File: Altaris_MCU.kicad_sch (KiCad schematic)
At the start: 47 parts, among them J1 Screw_Terminal_01x02, J2 Conn_01x04_Pin, J3 Screw_Terminal_01x02, J4 Screw_Terminal_01x02, J5 Conn_01x04_Pin, J6 Conn_01x04_Pin, J7 Conn_01x08_Socket, SW2 RESET1, SW3 BOOT1, U1 ESP32-S3-WROOM-1, U2 MAX31855KASA, U3 TPS79333-EP, U4 ICM-20948, U5 TPS79318-EP, U6 SN74AVC4T774RSVR, U7 MAX31855KASA, U8 MAX31855KASA

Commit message: Added USB-C to Schematic and PCB Layout
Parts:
- added C24, C25: 0.1uF, Capacitor_SMD:C_0402_1005Metric_Pad0.74x0.62mm_HandSolder, symbol Device:C
- added C26, C29: 100n, Capacitor_SMD:C_0402_1005Metric, symbol Device:C
- added C27, C28, C30: 10u, Capacitor_SMD:C_0402_1005Metric, symbol Device:C
- added FB3: 600/100, Resistor_SMD:R_0805_2012Metric, symbol Device:R
- added J8: Screw_Terminal_01x02, TerminalBlock:TerminalBlock_MaiXu_MX126-5.0-02P_1x02_P5.00mm, symbol Connector:Screw_Terminal_01x02
- added J9: USB_C_Receptacle_USB2.0_16P, Connector_USB:USB_C_Receptacle_HRO_TYPE-C-31-M-12, symbol Connector:USB_C_Receptacle_USB2.0_16P
- added R4, R5: 5.1k, Resistor_SMD:R_0402_1005Metric, symbol Device:R
- added U10: USBLC6-2SC6, Package_TO_SOT_SMD:SOT-23-6, symbol Power_Protection:USBLC6-2SC6
- added U11: SPX3819M5-L-3-3, Package_TO_SOT_SMD:SOT-23-5, symbol Regulator_Linear:SPX3819M5-L-3-3
- added U9: SN74AVC4T774RSVR, MyFootprints:RSV0016A, symbol SN74AVC4T774RSVR:SN74AVC4T774RSVR
- C1, C10, C15, C22, C23, C4, C5, C6, C7, C8, C9: footprint Capacitors:C_0805_2012Metric_Pad1.18x1.45mm_HandSolder -> Capacitor_SMD:C_0805_2012Metric_Pad1.18x1.45mm_HandSolder
- J1, J3, J4: footprint (none) -> TerminalBlock:TerminalBlock_MaiXu_MX126-5.0-02P_1x02_P5.00mm
- J2, J5, J6: footprint (none) -> TerminalBlock:TerminalBlock_MaiXu_MX126-5.0-04P_1x04_P5.00mm
- U4: footprint ICM-20948:QFN24_3X3X0P9_IVS -> MyFootprints:QFN24_3X3X0P9_IVS
- U6: footprint LEVELSHIFTER:QFN40P260X180X55-16N -> MyFootprints:RSV0016A
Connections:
- net T+ is gone; now on net T1+: U7.3 (T+)
- net T- is gone; now on net T1-: U7.2 (T-)
- net +1.8V: now also C25.1, U9.13 (VCCB)
- net +3.3V_b: now also R10.2, R9.2, C24.1, C30.1, U11.5 (OUT), U9.14 (VCCA), U9.16 (DIR2), U9.5 (DIR3), U9.6 (DIR4)
- net +5V_b: now also J8.1 (Pin_1)
- net ADC_IN1: now also U1.24 (IO47); no longer U1.39 (IO1)
- net ADC_IN2: now also U1.25 (IO48); no longer U1.38 (IO2)
- net ADC_IN3: now also U1.26 (IO45); no longer U1.15 (IO3)
- net CLK: now also U1.35 (IO42); no longer U1.22 (IO14)
- net ESP32_EN: now also C18.1, R9.1
- net GND: now also C24.2, C25.2, C26.2, C27.2, C28.2, C29.2, C30.2, J8.2 (Pin_2), J9.A1 (GND), J9.A12 (GND), J9.B1 (GND), J9.B12 (GND), J9.S1 (SHIELD), R4.2, R5.2, U10.2 (GND), U11.2 (GND), U9.15 (DIR1), U9.7 (~{OE}), U9.8 (GND)
- net GPIO0: now also C19.1, R10.1
- net ICM_CS: now also U1.38 (IO2); no longer U1.8 (IO15)
- net ICM_FSYNC: now also U1.33 (IO40), U9.1 (A1); no longer U1.9 (IO16)
- net ICM_FSYNC_1.8V: now also U9.12 (B1)
- net ICM_INT: now also U1.32 (IO39), U9.2 (A2); no longer U1.19 (IO11)
- net ICM_INT_1.8V: now also U9.11 (B2)
- net MAX_CS2: now also U1.18 (IO10); no longer U1.12 (IO8)
- net MAX_CS3: now also U1.19 (IO11); no longer U1.18 (IO10)
- net MISO: now also U1.39 (IO1); no longer U1.20 (IO12)
- net MOSI: now also U1.34 (IO41); no longer U1.21 (IO13)
- net T1-: no longer U2.2 (T-)
- net T2-: now also U2.2 (T-)
- net Common2: now reaches J2.2 (Pin_2)
- net Common3: now reaches J5.2 (Pin_2)
- net Common1: now reaches J6.2 (Pin_2)
- net USB-: now reaches U1.13 (USB_D-)
- net USB-: now also U10.6 (I/O1)
- net USB+: now reaches U1.14 (USB_D+)
- net USB+: now also U10.4 (I/O2)
- new net: J9.B5 (CC2), R4.1
- new net: C29.1, U11.4 (BP)
- new net: J9.A5 (CC1), R5.1
- new net: J9.A7 (D-), J9.B7 (D-), U10.1 (I/O1)
- new net: J9.A6 (D+), J9.B6 (D+), U10.3 (I/O2)
- new net +VBUS: C26.1, FB3.2, J9.A4 (VBUS), J9.A9 (VBUS), J9.B4 (VBUS), J9.B9 (VBUS), U10.5 (VBUS)
- new net +VBUSF: C27.1, C28.1, FB3.1, U11.1 (IN), U11.3 (EN)
- no-connect marks 24 -> 29
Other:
- moved on the sheet: C1, C10, C11, C12, C13, C14, C15, C16, C17, C18, C19, C2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

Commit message: Added Buck Converter to Schematic
USB-C BUS(5V) -> BUCK -> 3.3V -> (Voltage regulator to get 1.8V?)
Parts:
- added C31: 4.7u, Capacitor_SMD:C_0201_0603Metric, symbol Device:C
- added C32: 20u, Capacitor_SMD:C_0201_0603Metric, symbol Device:C
- added C33: 120p, Capacitor_SMD:C_0201_0603Metric, symbol Device:C
- added L1: L, Inductor_SMD:L_6.3x6.3_H3, symbol Device:L
- added R6, R8: 100k, Resistor_SMD:R_0402_1005Metric, symbol Device:R_Small
- added R7: 450k, Resistor_SMD:R_0402_1005Metric, symbol Device:R_Small
- added U12: TPS62827DMQT, MyFootprints:DMQ0006A, symbol BuckConverter:TPS62827DMQT
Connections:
- net +3.3V_b: now also C32.1, C33.1, L1.2, R7.2
- net GND: now also C31.1, C32.2, C33.2, R7.1, R8.1, R8.2, U12.3 (FB), U12.4 (GND)
- new net: R6.1, U12.2 (PG)
- new net: L1.1, U12.5 (SW)
- new net VBUS: C31.2, R6.2, U12.1 (EN), U12.6 (VIN)
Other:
- moved on the sheet: C1, C10, C11, C12, C13, C16, C17, C24, C25, C4, C5, C6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

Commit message: added second USB port, labels, organize
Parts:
- added C39, C40, C41: 0.1uF, Capacitor_SMD:C_0402_1005Metric_Pad0.74x0.62mm_HandSolder, symbol Device:C
- added D1: 1N4148WT, Diode_SMD:D_SOD-523, symbol Diode:1N4148WT
- added J10: USB_C_Receptacle_USB2.0_16P, Connector_USB:USB_C_Receptacle_HRO_TYPE-C-31-M-12, symbol Connector:USB_C_Receptacle_USB2.0_16P
- added Q1: Q_NMOS, symbol Device:Q_NMOS
- added R13, R14: 5.1k, Resistor_SMD:R_0402_1005Metric, symbol Device:R
- added U15: CH340X, Package_SO:MSOP-10_3x3mm_P0.5mm, symbol Interface_USB:CH340X
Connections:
- net +3.3V_b: now also C41.2, Q1.G
- net +VBUS: now also C40.1, J10.A4 (VBUS), J10.A7 (D-), J10.A9 (VBUS), J10.B4 (VBUS), J10.B9 (VBUS), U15.7 (VCC)
- net GND: now also C39.1, C40.2, C41.1, J10.A1 (GND), J10.A12 (GND), J10.B1 (GND), J10.B12 (GND), J10.B6 (D+), J10.S1 (SHIELD), R13.2, R14.2, U15.3 (GND)
- net RXD0: now reaches U1.36 (RXD0)
- net RXD0: now also D1.2 (A)
- net TXD0: now reaches U1.37 (TXD0)
- net TXD0: now also Q1.S
- new net: J10.B5 (CC2), R13.1
- new net: C39.2, U15.10 (V3)
- new net: D1.1 (K), U15.8 (TXD)
- new net: Q1.D, U15.9 (RXD)
- new net: J10.A5 (CC1), R14.1
- new net UD+: J10.A6 (D+), U15.1 (UD+)
- new net UD-: J10.B7 (D-), U15.2 (UD-)
- no-connect marks 29 -> 32
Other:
- note added: "2SK3018"
- note added: "3871K519 Thermocouples"
- note added: "4/13/26"
- note added: "Debug"
- note added: "ESP 32"
- note added: "LDO Voltage Regulators"
- note added: "Level Shifters for IMU"
- note added: "Pressure Sensors"
- note added: "Standard Panel Jacks"
- note added: "Step-down Converter"
- note added: "Thermocouple-to-Digital Converters:"
- note added: "USB to Serial Port Chip"
- note added: "USB-C Ports"
- note removed: "3871K519 Thermocouple"
- note removed: "4/7/26"
- note removed: "ESP32"
- note removed: "Pressure Sensor"
- note removed: "Standard Panel Jack"
- moved on the sheet: C1, C10, C11, C12, C13, C14, C15, C16, C17, C20, C21, C22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

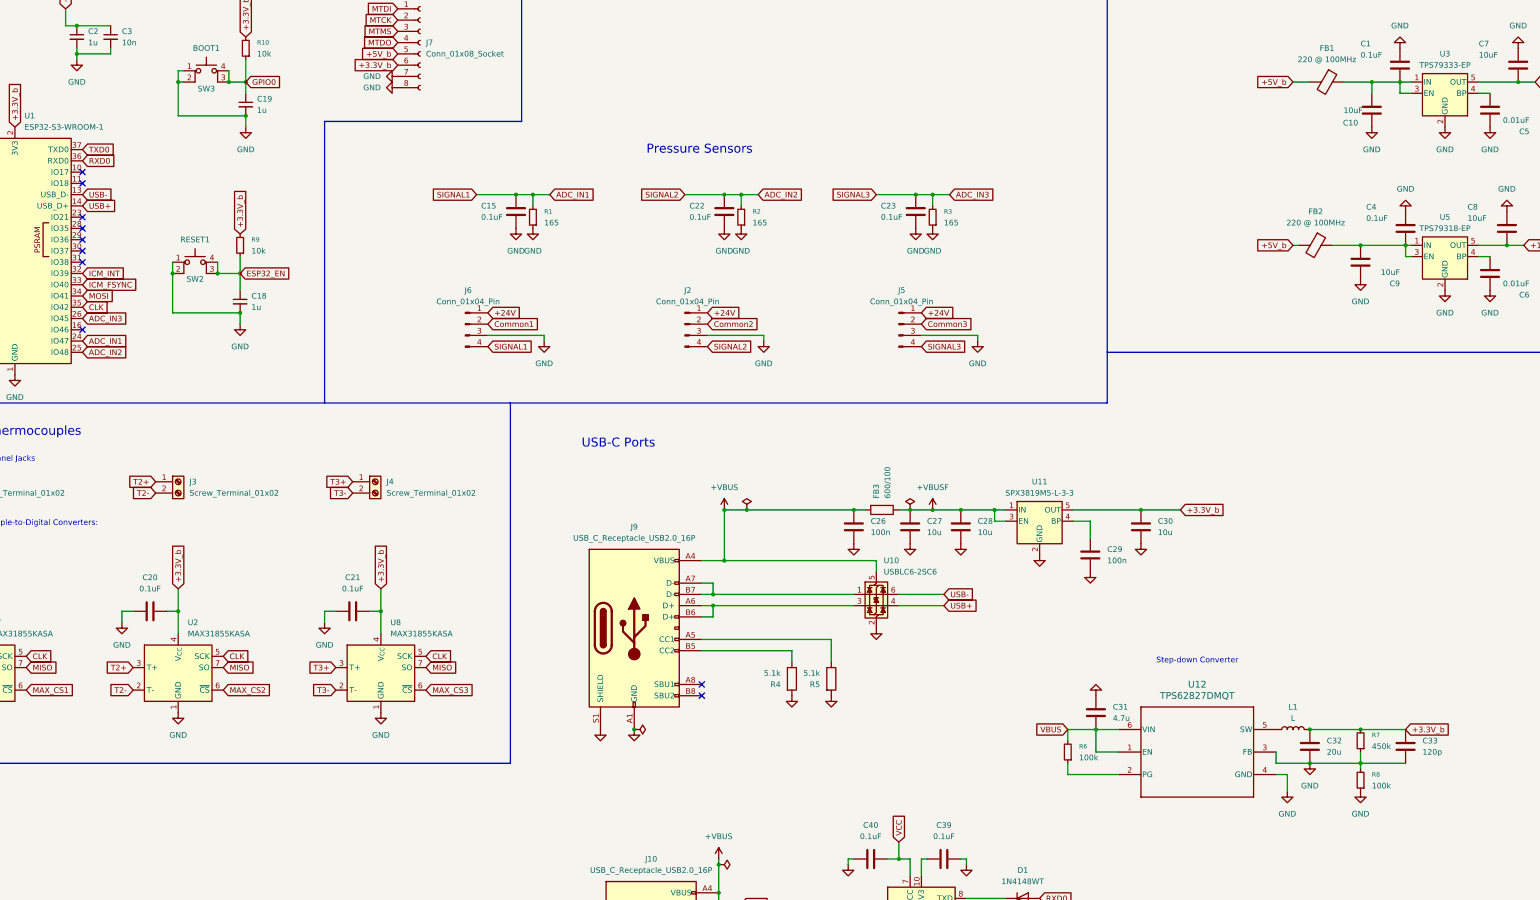
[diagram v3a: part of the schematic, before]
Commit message: Swapped LDO for Buck and added some test LED's
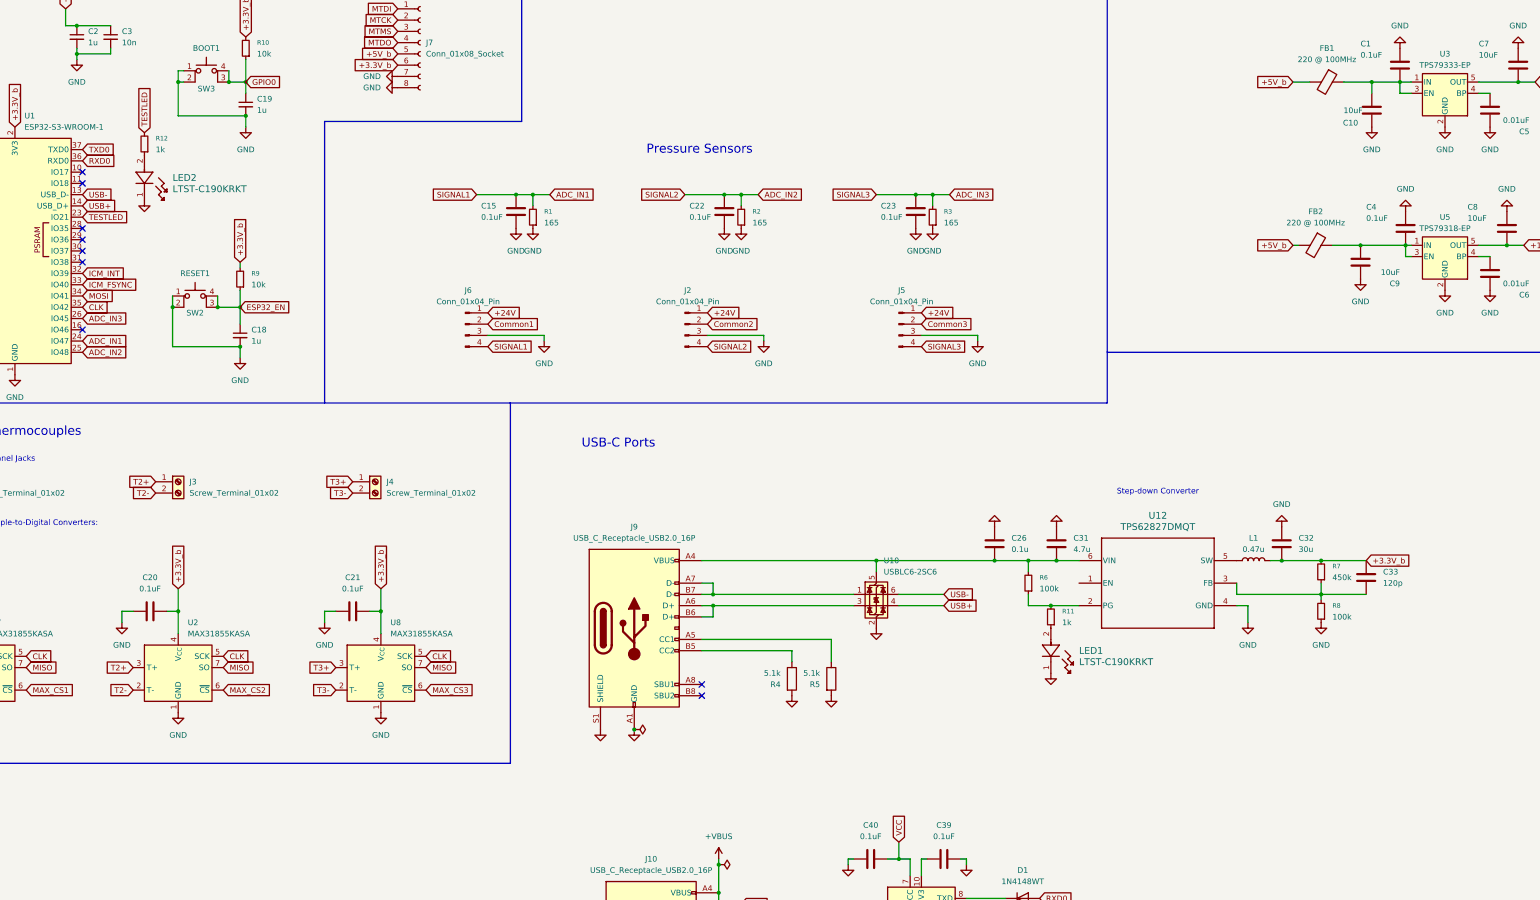
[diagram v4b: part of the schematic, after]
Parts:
- removed C27, C28, C30: 10u, Capacitor_SMD:C_0402_1005Metric, symbol Device:C
- removed C29: 100n, Capacitor_SMD:C_0402_1005Metric, symbol Device:C
- removed FB3: 600/100, Resistor_SMD:R_0805_2012Metric, symbol Device:R
- removed U11: SPX3819M5-L-3-3, Package_TO_SOT_SMD:SOT-23-5, symbol Regulator_Linear:SPX3819M5-L-3-3
- added LED1, LED2: LTST-C190KRKT, MyFootprints:LED_LTST-C190_LTO, symbol LED:LTST-C190KRKT
- added R11, R12: 1k, Resistor_SMD:R_0402_1005Metric, symbol Device:R_Small
- C26: value 100n -> 0.1u; footprint Capacitor_SMD:C_0402_1005Metric -> Capacitor_SMD:C_0201_0603Metric
- C32: value 20u -> 30u
- L1: value L -> 0.47u; footprint Inductor_SMD:L_6.3x6.3_H3 -> MyFootprints:IND_XFL4015_COC
- Q1: footprint (none) -> Package_TO_SOT_SMD:SOT-23
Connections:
- net +VBUS: no longer C26.1, J9.A4 (VBUS), J9.A9 (VBUS), J9.B4 (VBUS), J9.B9 (VBUS), U10.5 (VBUS)
- net GND: now also C26.1, LED1.1, LED2.1; no longer C26.2, C33.2, R7.1, R8.2, U12.3 (FB)
- net at R6.1, U12.2 (PG): now also R11.2
- net TESTLED: now reaches U1.23 (IO21)
- net TESTLED: now also R12.2
- net VBUS: no longer names the net of C31.2, R6.2, U12.6 (VIN)
- net VBUS: now also C26.2, J9.A4 (VBUS), J9.A9 (VBUS), J9.B4 (VBUS), J9.B9 (VBUS), U10.5 (VBUS); no longer U12.1 (EN)
- new net: LED2.2, R12.1
- new net: LED1.2, R11.1
- new net: C33.2, R7.1, R8.2, U12.3 (FB)
- no-connect marks 32 -> 31
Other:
- moved on the sheet: C18, C31, C32, C33, L1, R6, R7, R8, R9, SW2, U12

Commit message: Moved USB-C, Routed Buck converter output to LDO, Removed an LDO on PCB, Added another Thermocouple sensor
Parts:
- removed J2, J5: Conn_01x04_Pin, TerminalBlock:TerminalBlock_MaiXu_MX126-5.0-04P_1x04_P5.00mm, symbol Connector:Conn_01x04_Pin
- added C27: 0.1uF, Capacitor_SMD:C_0402_1005Metric_Pad0.74x0.62mm_HandSolder, symbol Device:C
- added J11: Screw_Terminal_01x02, TerminalBlock:TerminalBlock_MaiXu_MX126-5.0-02P_1x02_P5.00mm, symbol Connector:Screw_Terminal_01x02
- added J2, J5: Conn_01x04_Pin, TerminalBlock:TerminalBlock_MaiXu_MX126-5.0-02P_1x02_P5.00mm, symbol Connector:Conn_01x02_Pin
- added U11: MAX31855KASA, Package_SO:SOIC-8_3.9x4.9mm_P1.27mm, symbol Sensor_Temperature:MAX31855KASA
- J6: footprint TerminalBlock:TerminalBlock_MaiXu_MX126-5.0-04P_1x04_P5.00mm -> TerminalBlock:TerminalBlock_MaiXu_MX126-5.0-02P_1x02_P5.00mm; symbol Connector:Conn_01x04_Pin -> Connector:Conn_01x02_Pin
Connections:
- net +24V is gone; now on net Common1: J6.1 (Pin_1)
- net +3.3V_b: now also FB2.2, C27.1, U11.4 (V_{CC})
- net +5V_b: no longer FB2.2
- net ADC_IN1: now also J6.2 (Pin_2); no longer J6.4 (Pin_4)
- net ADC_IN2: now also J2.2 (Pin_2)
- net ADC_IN3: now also J5.2 (Pin_2)
- net CLK: now also U11.5 (SCK)
- net Common1: no longer J6.2 (Pin_2)
- net Common2: now also J2.1 (Pin_1)
- net Common3: now also J5.1 (Pin_1)
- net GND: now also C27.2, U11.1 (GND); no longer J6.3 (Pin_3)
- net MISO: now also U11.7 (SO)
- net MAX_CS4: now reaches U1.20 (IO12)
- net MAX_CS4: now also U11.6 (~{CS})
- new net T4+: J11.1 (Pin_1), U11.3 (T+)
- new net T4-: J11.2 (Pin_2), U11.2 (T-)
- no-connect marks 31 -> 30
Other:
- note added: "WILL PROBOLY GET RID OF THIS LDO"
- moved on the sheet: C1, C10, C26, C31, C32, C33, C39, C40, C41, C5, C7, D1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
